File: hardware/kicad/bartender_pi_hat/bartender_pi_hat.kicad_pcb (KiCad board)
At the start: 2 copper layers, 23 x 55 mm, 5 parts, among them J1 Raspberry_Pi, J3 Pump Connector, J4 Scale Connector, J5 12V Output

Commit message: Changes for RPi LED Controller
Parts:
- added J6: LED Connector, Connector_JST:JST_XH_B3B-XH-A_1x03_P2.50mm_Vertical, F.Cu at (76.2, 88.9)
- moved REF** 12.3 mm to (76.5, 95.8)
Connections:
- J1 pad 10: Net-(J1-Pad10) -> unconnected-(J1-Pad10)
- J1 pad 11: Net-(J1-Pad11) -> unconnected-(J1-Pad11)
- J1 pad 14: Net-(J1-Pad14) -> unconnected-(J1-Pad14)
- J1 pad 17: Net-(J1-Pad17) -> unconnected-(J1-Pad17)
- J1 pad 18: Net-(J1-Pad18) -> unconnected-(J1-Pad18)
- J1 pad 19: Net-(J1-Pad19) -> unconnected-(J1-Pad19)
- J1 pad 20: Net-(J1-Pad20) -> unconnected-(J1-Pad20)
- J1 pad 21: Net-(J1-Pad21) -> unconnected-(J1-Pad21)
- J1 pad 22: Net-(J1-Pad22) -> unconnected-(J1-Pad22)
- J1 pad 23: Net-(J1-Pad23) -> unconnected-(J1-Pad23)
- J1 pad 24: Net-(J1-Pad24) -> unconnected-(J1-Pad24)
- J1 pad 25: Net-(J1-Pad25) -> unconnected-(J1-Pad25)
- J1 pad 26: Net-(J1-Pad26) -> unconnected-(J1-Pad26)
- J1 pad 27: Net-(J1-Pad27) -> unconnected-(J1-Pad27)
- J1 pad 28: Net-(J1-Pad28) -> unconnected-(J1-Pad28)
- J1 pad 3: Net-(J1-Pad3) -> unconnected-(J1-Pad3)
- J1 pad 30: Net-(J1-Pad30) -> unconnected-(J1-Pad30)
- J1 pad 33: Net-(J1-Pad33) -> unconnected-(J1-Pad33)
- J1 pad 34: Net-(J1-Pad34) -> unconnected-(J1-Pad34)
- J1 pad 4: Net-(J1-Pad4) -> Net-(J1-Pad2)
- J1 pad 5: Net-(J1-Pad5) -> unconnected-(J1-Pad5)
- J1 pad 6: Net-(J1-Pad6) -> unconnected-(J1-Pad6)
- J1 pad 8: Net-(J1-Pad8) -> unconnected-(J1-Pad8)
- J1 pad 9: Net-(J1-Pad9) -> unconnected-(J1-Pad9)
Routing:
- net Net-(J1-Pad12): track 0.00 -> 31.1 mm
- net Net-(J1-Pad2): track 0.00 -> 29.6 mm
- added copper zone on F.Cu, net GND
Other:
- net class Default removed
- board text added: "Bartender v1.3 - Raspberry Pi Hat github.com/dburnsii/bartender"
- board text removed: "Bartender v1.2 - Raspberry Pi Hat github.com/dburnsii/bartender"

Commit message: Update GND for all RPi Pins
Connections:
- J1 pad 14: unconnected-(J1-Pad14) -> GND
- J1 pad 20: unconnected-(J1-Pad20) -> GND
- J1 pad 25: unconnected-(J1-Pad25) -> GND
- J1 pad 30: unconnected-(J1-Pad30) -> GND
- J1 pad 34: unconnected-(J1-Pad34) -> GND
- J1 pad 6: unconnected-(J1-Pad6) -> GND
- J1 pad 9: unconnected-(J1-Pad9) -> GND

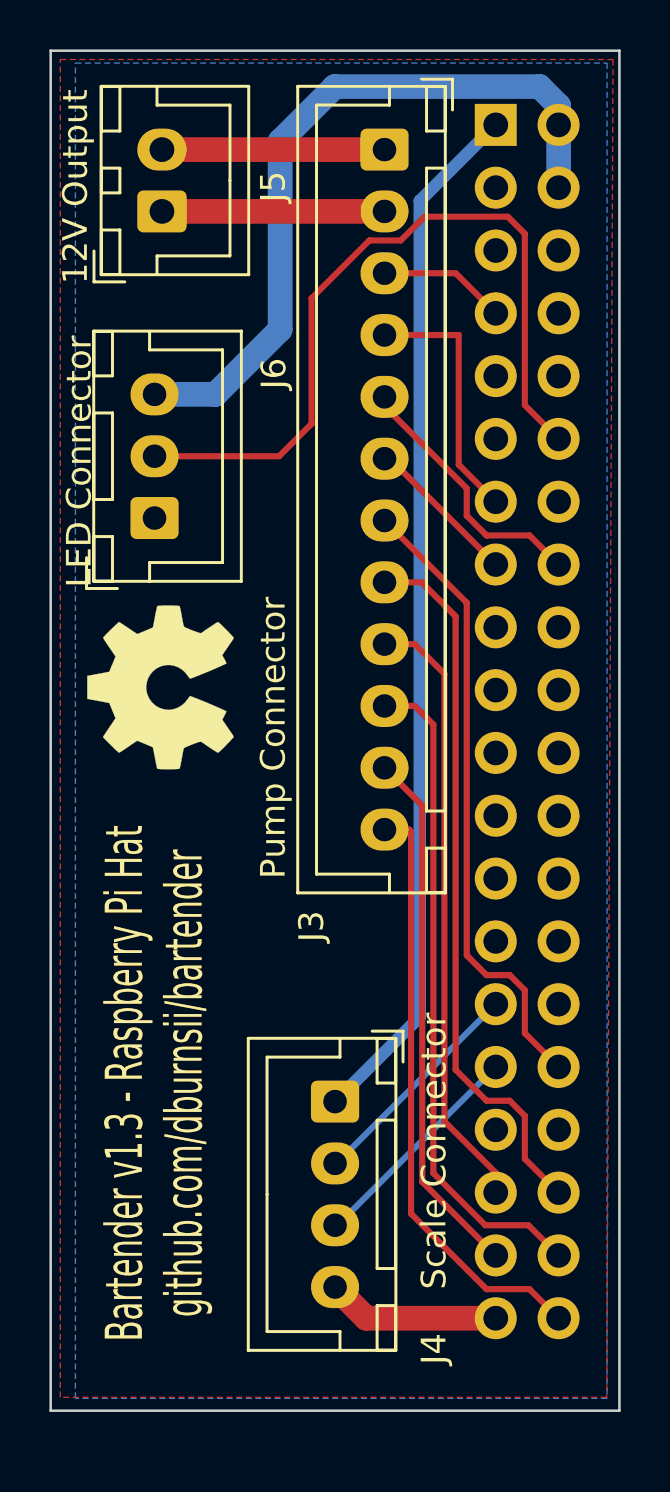
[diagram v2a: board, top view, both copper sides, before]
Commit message: Update to pull scale and valve from config, update boards
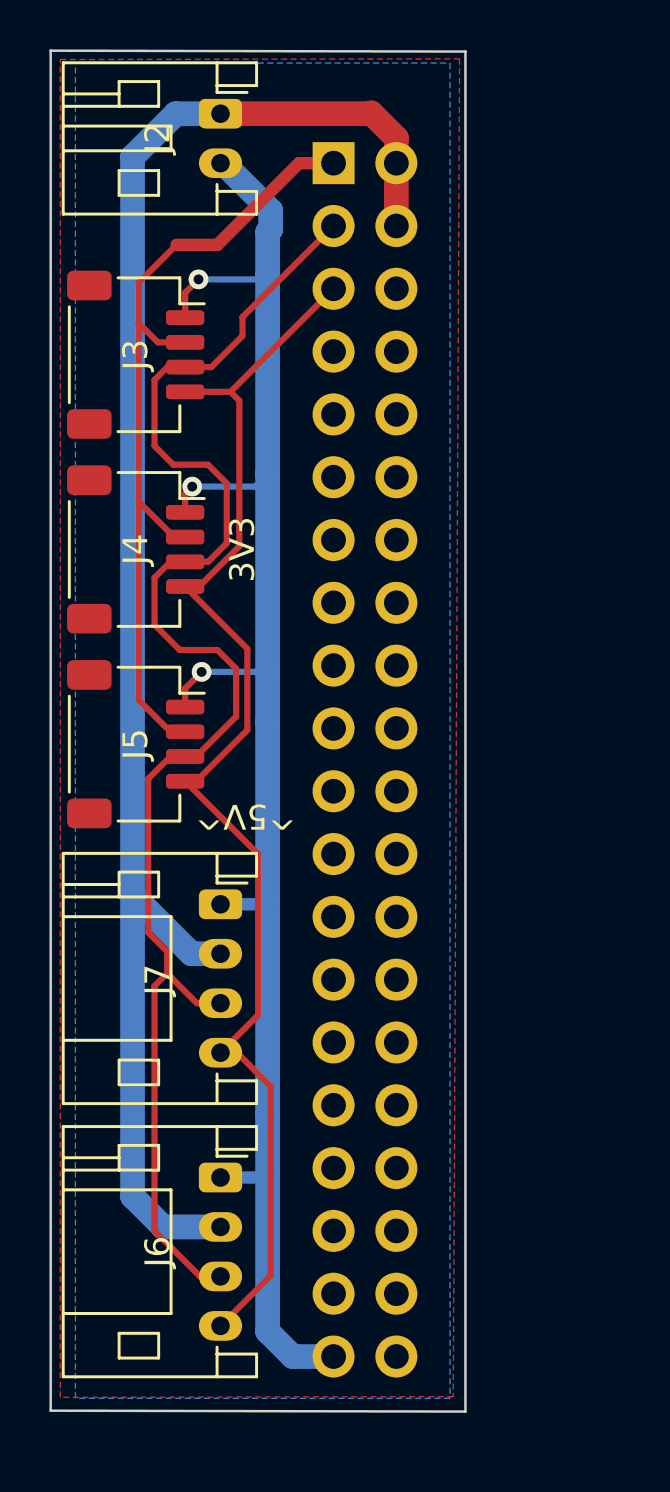
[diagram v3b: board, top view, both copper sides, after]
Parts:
- removed REF**: OSHW-Symbol_6.7x6mm_SilkScreen, Symbol:OSHW-Symbol_6.7x6mm_SilkScreen
- added J2: 5v - JST-PH, Connector_JST:JST_PH_S2B-PH-K_1x02_P2.00mm_Horizontal, F.Cu at (78.9, 72.5)
- added J7: Stemma, Connector_JST:JST_PH_S4B-PH-K_1x04_P2.00mm_Horizontal, F.Cu at (78.9, 104.5)
- J3: value Pump Connector -> Conn_01x04_Female; footprint Connector_JST:JST_XH_B12B-XH-A_1x12_P2.50mm_Vertical -> Connector_JST:JST_SH_SM04B-SRSS-TB_1x04-1MP_P1.00mm_Horizontal
- J4: value Scale Connector -> Conn_01x04_Female; footprint Connector_JST:JST_XH_B4B-XH-A_1x04_P2.50mm_Vertical -> Connector_JST:JST_SH_SM04B-SRSS-TB_1x04-1MP_P1.00mm_Horizontal
- J5: value 12V Output -> Conn_01x04_Female; footprint Connector_JST:JST_XH_B2B-XH-A_1x02_P2.50mm_Vertical -> Connector_JST:JST_SH_SM04B-SRSS-TB_1x04-1MP_P1.00mm_Horizontal
- J6: value LED Connector -> Stemma; footprint Connector_JST:JST_XH_B3B-XH-A_1x03_P2.50mm_Vertical -> Connector_JST:JST_PH_S4B-PH-K_1x04_P2.00mm_Horizontal
- moved J6 26.8 mm to (78.9, 115.6), turned to -90 degrees
- moved J4 23.7 mm to (75.4, 90.2)
- moved J5 21.6 mm to (75.4, 98.0), turned to -90 degrees
- moved J3 13.0 mm to (75.4, 82.3)
- moved J1 6.74 mm to (83.4, 74.5)
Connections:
- J1 pad 1: /3v3 -> +3V3
- J1 pad 12: Net-(J1-Pad12) -> unconnected-(J1-Pad12)
- J1 pad 13: /Pump9 -> unconnected-(J1-Pad13)
- J1 pad 15: /Pump7 -> unconnected-(J1-Pad15)
- J1 pad 16: /Pump8 -> unconnected-(J1-Pad16)
- J1 pad 2: Net-(J1-Pad2) -> +5V
- J1 pad 29: /DT -> unconnected-(J1-Pad29)
- J1 pad 3: unconnected-(J1-Pad3) -> Net-(J3-Pad3)
- J1 pad 31: /Scale_SCK -> unconnected-(J1-Pad31)
- J1 pad 32: /Pump6 -> unconnected-(J1-Pad32)
- J1 pad 35: /Pump4 -> unconnected-(J1-Pad35)
- J1 pad 36: /Pump5 -> unconnected-(J1-Pad36)
- J1 pad 37: /Pump2 -> unconnected-(J1-Pad37)
- J1 pad 38: /Pump3 -> unconnected-(J1-Pad38)
- J1 pad 4: Net-(J1-Pad2) -> +5V
- J1 pad 40: /Pump1 -> unconnected-(J1-Pad40)
- J1 pad 5: unconnected-(J1-Pad5) -> Net-(J3-Pad4)
- J1 pad 7: /Pump10 -> unconnected-(J1-Pad7)
- J3 pad 2: /12v -> +3V3
- J3 pad 3: /Pump10 -> Net-(J3-Pad3)
- J3 pad 4: /Pump9 -> Net-(J3-Pad4)
- J4 pad 1: /3v3 -> GND
- J4 pad 2: /DT -> +3V3
- J4 pad 3: /Scale_SCK -> Net-(J3-Pad3)
- J4 pad 4: GND -> Net-(J3-Pad4)
- J5 pad 1: /12v -> GND
- J5 pad 2: GND -> +3V3
- J6 pad 2: Net-(J1-Pad12) -> +5V
- J6 pad 3: Net-(J1-Pad2) -> Net-(J3-Pad3)
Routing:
- net +5V: track 0.00 -> 66.0 mm
- net Net-(J3-Pad3): track 0.00 -> 59.8 mm
- net GND: track 16.0 -> 69.3 mm, vias 0 -> 3
- net Net-(J3-Pad4): track 0.00 -> 53.2 mm
- net /3v3: track 42.2 -> 0.00 mm
- net +3V3: track 0.00 -> 33.5 mm
- net Net-(J1-Pad12): track 31.1 -> 0.00 mm
- net Net-(J1-Pad2): track 29.6 -> 0.00 mm
- net /Pump5: track 29.0 -> 0.00 mm
- net /Pump3: track 26.9 -> 0.00 mm
- net /Pump6: track 25.6 -> 0.00 mm
- net /Pump4: track 24.8 -> 0.00 mm
- net /Pump1: track 24.3 -> 0.00 mm
- net /Pump2: track 21.6 -> 0.00 mm
- net /Pump8: track 10.7 -> 0.00 mm
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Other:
- board size 23 x 55 mm -> 16.8 x 55 mm
- board text added: "3V3"
- board text added: "Bartender v1.4 - Raspberry Pi Hat github.com/dburnsii/bartender"
- board text added: "^5V^"
- board text removed: "Bartender v1.3 - Raspberry Pi Hat github.com/dburnsii/bartender"
